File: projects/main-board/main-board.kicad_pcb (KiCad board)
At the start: 2 copper layers, 1 part, among them J4 TC2030

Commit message: Add footprints and 3D models
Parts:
- added J5: NHD-4.3-480272EF-ASXP (Molex 54104-4031), footprint-library:Molex 54104-4031, F.Cu at (134.6, 64.8)

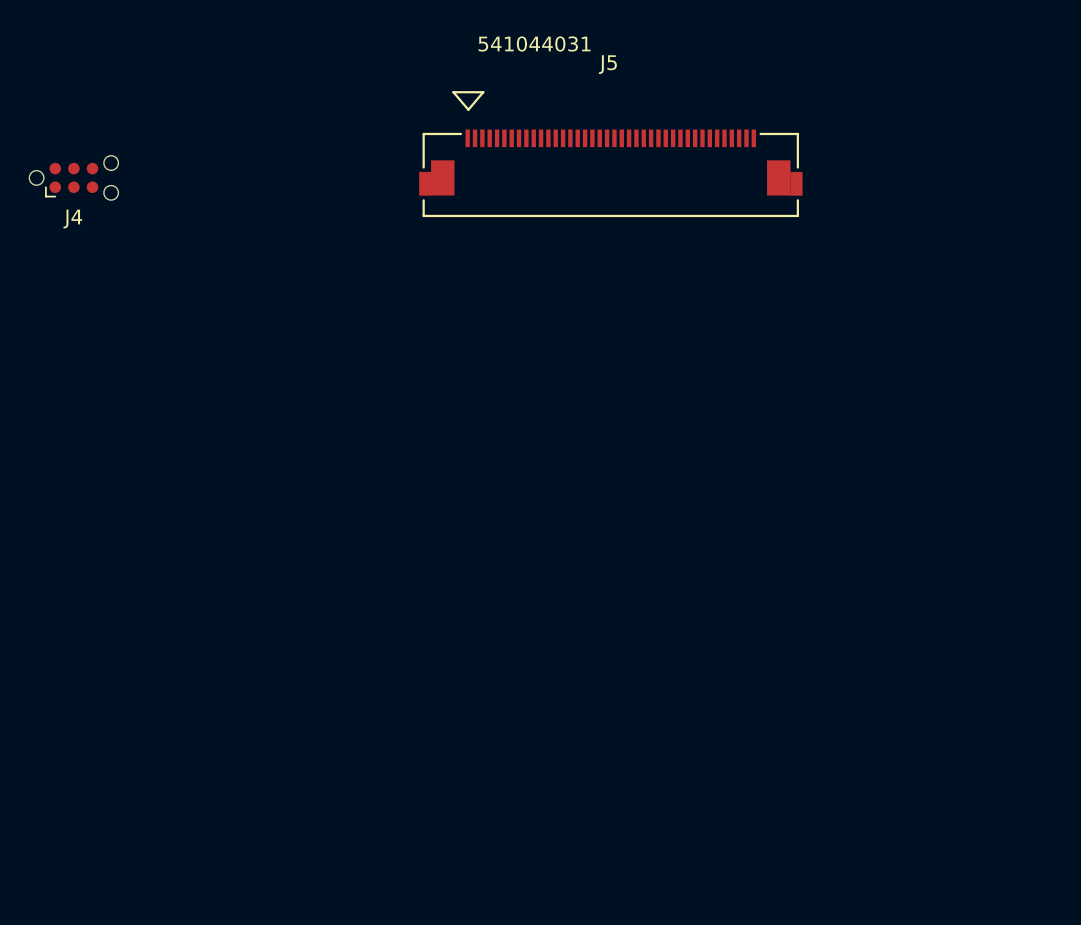
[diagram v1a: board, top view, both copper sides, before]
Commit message: Re-annotate schematics.
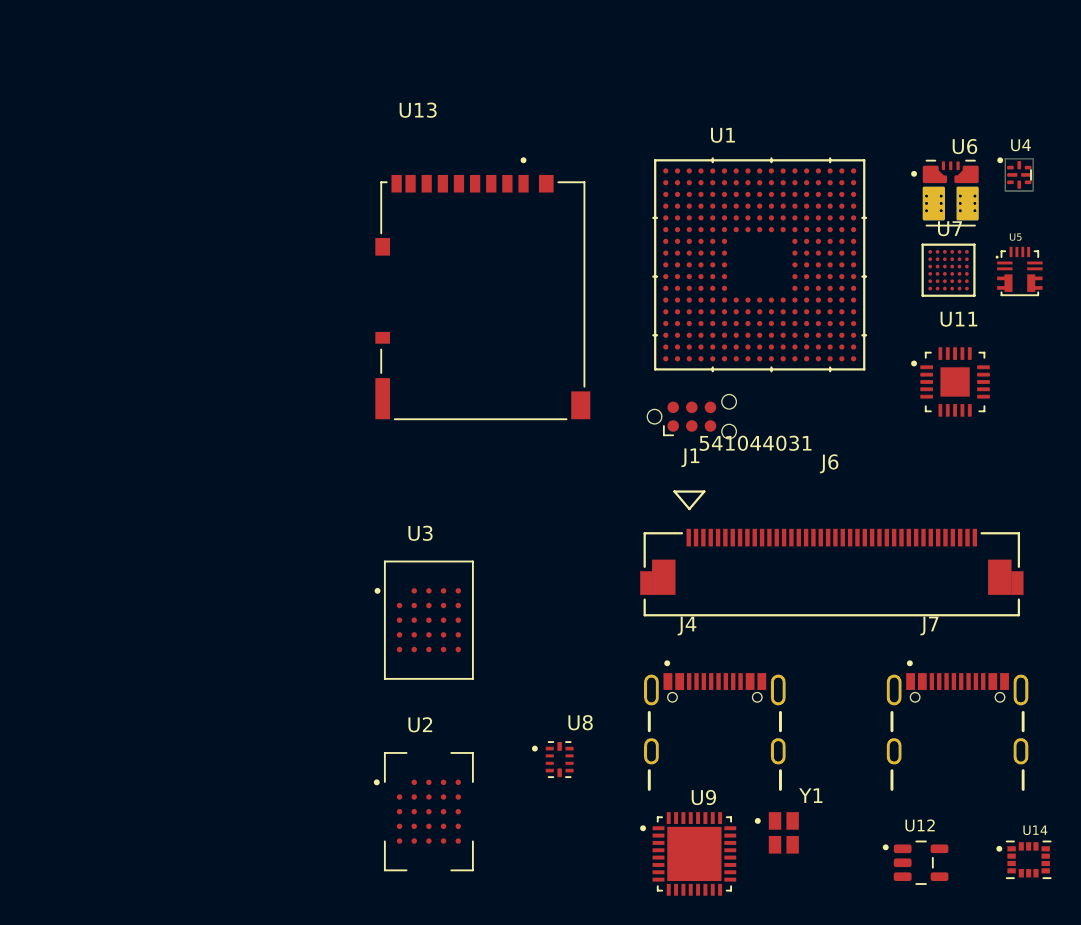
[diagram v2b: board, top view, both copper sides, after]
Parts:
- removed J5: NHD-4.3-480272EF-ASXP (Molex 54104-4031), footprint-library:Molex 54104-4031
- added J1: TC2030, Connector:Tag-Connect_TC2030-IDC-NL_2x03_P1.27mm_Vertical, F.Cu at (140.1, 81.3)
- added J6: NHD-4.3-480272EF-ASXP (Molex 54104-4031), footprint-library:Molex 54104-4031, F.Cu at (149.6, 92.0)
- added J7: USB4105-GF-A, footprint-library:USB4105-GF-A, F.Cu at (158.2, 104.1)
- added U1: STM32N657X0HxQ, footprint-library:STM32N645A0HxQ, F.Cu at (144.7, 70.9)
- added U11: NAU8325YG, footprint-library:NAU8325YG, F.Cu at (158.0, 78.9)
- added U12: TLV74330PDBVR, footprint-library:TLV74330PDBVR, F.Cu at (155.7, 111.7)
- added U13: DM3AT-SF-PEJM5, footprint-library:DM3AT-SF-PEJM5, F.Cu at (125.8, 73.4)
- added U14: LSM6DSO32TR, footprint-library:LSM6DSO32TR, F.Cu at (163.0, 111.5)
- added U2: APS256XXN-OBR-BG, footprint-library:APS256XXN-OBR-BG, F.Cu at (122.2, 108.2)
- added U3: MX25UM25645GXDI00, footprint-library:MX25UM25645GXDI00, F.Cu at (122.2, 95.1)
- added U4: TPS22992RXPR, footprint-library:TPS22992RXPR, F.Cu at (162.4, 64.8)
- added U5: MPM3805GQB-18-Z, footprint-library:MPM3805GQB-18-Z, F.Cu at (162.4, 71.5)
- added U6: TPSM863253RDXR, footprint-library:TPSM863253RDXR, F.Cu at (157.7, 66.1)
- added U7: MAX77972EWX+T, footprint-library:MAX77972EWX+T, F.Cu at (157.6, 71.3)
- added U8: TS3USB221ARSER, footprint-library:TS3USB221ARSER, F.Cu at (131.1, 104.6)
- added U9: ESP32-C6FH4, footprint-library:ESP32-C6FH4, F.Cu at (140.2, 111.1)
- added Y1: ABM10W-40.0000MHZ-8-B1U-T3, footprint-library:XTAL_ABM10W-40.0000MHZ-8-B1U-T3, F.Cu at (146.3, 109.6)
- J4: value TC2030 -> USB4105-GF-A; footprint Connector:Tag-Connect_TC2030-IDC-NL_2x03_P1.27mm_Vertical -> footprint-library:USB4105-GF-A
- moved J4 58.6 mm to (141.6, 104.1)

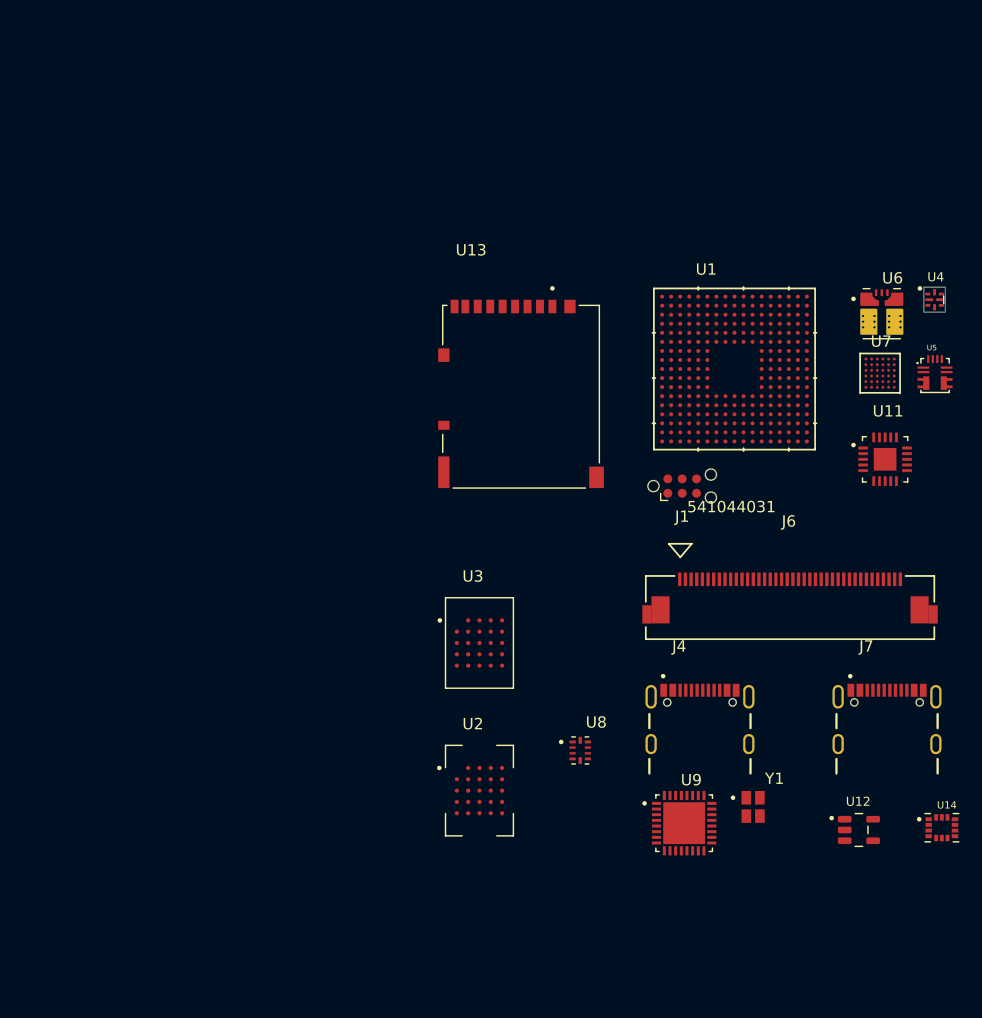
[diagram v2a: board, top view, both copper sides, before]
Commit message: Add footprints
- Inductors
- Switches
- Buttons
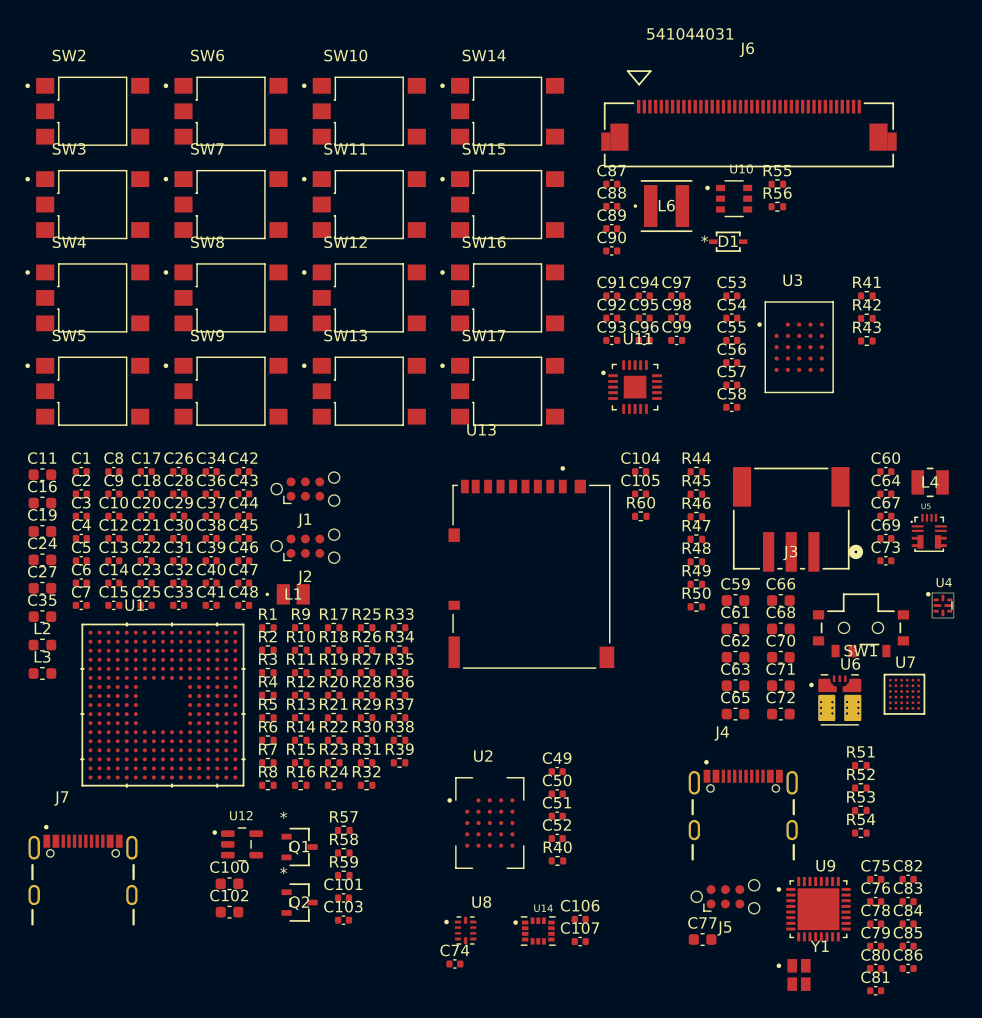
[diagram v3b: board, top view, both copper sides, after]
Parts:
- added C1: 100nF 10V, Capacitor_SMD:C_0402_1005Metric, F.Cu at (87.0, 80.0)
- added C10: 100nF 10V, Capacitor_SMD:C_0402_1005Metric, F.Cu at (89.8, 83.9)
- added C100: 10uF 10V, Capacitor_SMD:C_0603_1608Metric, F.Cu at (100.1, 116.4)
- added C101: 100nF 10V, Capacitor_SMD:C_0402_1005Metric, F.Cu at (110.1, 117.7)
- added C102: 10uF 10V, Capacitor_SMD:C_0603_1608Metric, F.Cu at (100.1, 118.9)
- added C103: 100nF 10V, Capacitor_SMD:C_0402_1005Metric, F.Cu at (110.1, 119.6)
- added C104: 100nF 10V, Capacitor_SMD:C_0402_1005Metric, F.Cu at (136.4, 80.0)
- added C105: 100nF 10V, Capacitor_SMD:C_0402_1005Metric, F.Cu at (136.4, 82.0)
- added C106: 100nF 10V, Capacitor_SMD:C_0402_1005Metric, F.Cu at (131.1, 119.5)
- added C107: 100nF 10V, Capacitor_SMD:C_0402_1005Metric, F.Cu at (131.1, 121.5)
- added C11: 22uF 10V, Capacitor_SMD:C_0603_1608Metric, F.Cu at (83.5, 80.2)
- added C12: 100nF 10V, Capacitor_SMD:C_0402_1005Metric, F.Cu at (89.8, 85.9)
- added C13: 100nF 10V, Capacitor_SMD:C_0402_1005Metric, F.Cu at (89.8, 87.9)
- added C14: 100nF 10V, Capacitor_SMD:C_0402_1005Metric, F.Cu at (89.8, 89.8)
- added C15: 100nF 10V, Capacitor_SMD:C_0402_1005Metric, F.Cu at (89.8, 91.8)
- added C16: 10uF 10V, Capacitor_SMD:C_0603_1608Metric, F.Cu at (83.5, 82.8)
- added C17: 1uF 10V, Capacitor_SMD:C_0402_1005Metric, F.Cu at (92.7, 80.0)
- added C18: 100nF 10V, Capacitor_SMD:C_0402_1005Metric, F.Cu at (92.7, 82.0)
- added C19: 22uF 10V, Capacitor_SMD:C_0603_1608Metric, F.Cu at (83.5, 85.3)
- added C2: 1uF 10V, Capacitor_SMD:C_0402_1005Metric, F.Cu at (87.0, 82.0)
- added C20: 1uF 10V, Capacitor_SMD:C_0402_1005Metric, F.Cu at (92.7, 83.9)
- added C21: 100nF 10V, Capacitor_SMD:C_0402_1005Metric, F.Cu at (92.7, 85.9)
- added C22: 1uF 10V, Capacitor_SMD:C_0402_1005Metric, F.Cu at (92.7, 87.9)
- added C23: 100nF 10V, Capacitor_SMD:C_0402_1005Metric, F.Cu at (92.7, 89.8)
- added C24: 10uF 10V, Capacitor_SMD:C_0603_1608Metric, F.Cu at (83.5, 87.8)
- added C25: 100nF 10V, Capacitor_SMD:C_0402_1005Metric, F.Cu at (92.7, 91.8)
- added C26: 100nF 10V, Capacitor_SMD:C_0402_1005Metric, F.Cu at (95.6, 80.0)
- added C27: 22uF 10V, Capacitor_SMD:C_0603_1608Metric, F.Cu at (83.5, 90.3)
- added C28: 100nF 10V, Capacitor_SMD:C_0402_1005Metric, F.Cu at (95.6, 82.0)
- added C29: 100nF 10V, Capacitor_SMD:C_0402_1005Metric, F.Cu at (95.6, 83.9)
- added C3: 2.2nF 10V, Capacitor_SMD:C_0402_1005Metric, F.Cu at (87.0, 83.9)
- added C30: 1uF 10V, Capacitor_SMD:C_0402_1005Metric, F.Cu at (95.6, 85.9)
- added C31: 100nF 10V, Capacitor_SMD:C_0402_1005Metric, F.Cu at (95.6, 87.9)
- added C32: 1uF 10V, Capacitor_SMD:C_0402_1005Metric, F.Cu at (95.6, 89.8)
- added C33: 100nF 10V, Capacitor_SMD:C_0402_1005Metric, F.Cu at (95.6, 91.8)
- added C34: 100nF 10V, Capacitor_SMD:C_0402_1005Metric, F.Cu at (98.4, 80.0)
- added C35: 22uF 10V, Capacitor_SMD:C_0603_1608Metric, F.Cu at (83.5, 92.8)
- added C36: 1uF 10V, Capacitor_SMD:C_0402_1005Metric, F.Cu at (98.4, 82.0)
- added C37: 1uF 10V, Capacitor_SMD:C_0402_1005Metric, F.Cu at (98.4, 83.9)
- added C38: 1uF 10V, Capacitor_SMD:C_0402_1005Metric, F.Cu at (98.4, 85.9)
- added C39: 1uF 10V, Capacitor_SMD:C_0402_1005Metric, F.Cu at (98.4, 87.9)
- added C4: 4.7uF 10V, Capacitor_SMD:C_0402_1005Metric, F.Cu at (87.0, 85.9)
- added C40: 100nF 10V, Capacitor_SMD:C_0402_1005Metric, F.Cu at (98.4, 89.8)
- added C41: 100nF 10V, Capacitor_SMD:C_0402_1005Metric, F.Cu at (98.4, 91.8)
- added C42: 100nF 10V, Capacitor_SMD:C_0402_1005Metric, F.Cu at (101.3, 80.0)
- added C43: 1uF 10V, Capacitor_SMD:C_0402_1005Metric, F.Cu at (101.3, 82.0)
- added C44: 100nF 10V, Capacitor_SMD:C_0402_1005Metric, F.Cu at (101.3, 83.9)
- added C45: 100nF 10V, Capacitor_SMD:C_0402_1005Metric, F.Cu at (101.3, 85.9)
- added C46: 1uF 10V, Capacitor_SMD:C_0402_1005Metric, F.Cu at (101.3, 87.9)
- added C47: 100nF 10V, Capacitor_SMD:C_0402_1005Metric, F.Cu at (101.3, 89.8)
- added C48: 1uF 10V, Capacitor_SMD:C_0402_1005Metric, F.Cu at (101.3, 91.8)
- added C49: 100nF 10V, Capacitor_SMD:C_0402_1005Metric, F.Cu at (129.0, 106.5)
- added C5: 100nF 10V, Capacitor_SMD:C_0402_1005Metric, F.Cu at (87.0, 87.9)
- added C50: 100nF 10V, Capacitor_SMD:C_0402_1005Metric, F.Cu at (129.0, 108.5)
- added C51: 4.7uF 10V, Capacitor_SMD:C_0402_1005Metric, F.Cu at (129.0, 110.4)
- added C52: 4.7uF 10V, Capacitor_SMD:C_0402_1005Metric, F.Cu at (129.0, 112.4)
- added C53: 4.7uF 10V, Capacitor_SMD:C_0402_1005Metric, F.Cu at (144.5, 64.4)
- added C54: 4.7uF 10V, Capacitor_SMD:C_0402_1005Metric, F.Cu at (144.5, 66.4)
- added C55: 4.7uF 10V, Capacitor_SMD:C_0402_1005Metric, F.Cu at (144.5, 68.4)
- added C56: 100nF 10V, Capacitor_SMD:C_0402_1005Metric, F.Cu at (144.5, 70.3)
- added C57: 100nF 10V, Capacitor_SMD:C_0402_1005Metric, F.Cu at (144.5, 72.3)
- added C58: 100nF 10V, Capacitor_SMD:C_0402_1005Metric, F.Cu at (144.5, 74.3)
- added C59: 10uF 10V, Capacitor_SMD:C_0603_1608Metric, F.Cu at (144.8, 91.4)
- added C6: 100nF 10V, Capacitor_SMD:C_0402_1005Metric, F.Cu at (87.0, 89.8)
- added C60: 100nF 10V, Capacitor_SMD:C_0402_1005Metric, F.Cu at (158.1, 80.0)
- added C61: 10uF 10V, Capacitor_SMD:C_0603_1608Metric, F.Cu at (144.8, 93.9)
- added C62: 10uF 10V, Capacitor_SMD:C_0603_1608Metric, F.Cu at (144.8, 96.4)
- added C63: 10uF 10V, Capacitor_SMD:C_0603_1608Metric, F.Cu at (144.8, 98.9)
- added C64: 2.2uF 10V, Capacitor_SMD:C_0402_1005Metric, F.Cu at (158.1, 82.0)
- added C65: 10uF 10V, Capacitor_SMD:C_0603_1608Metric, F.Cu at (144.8, 101.4)
- added C66: 10uF 10V, Capacitor_SMD:C_0603_1608Metric, F.Cu at (148.8, 91.4)
- added C67: 100nF 10V, Capacitor_SMD:C_0402_1005Metric, F.Cu at (158.1, 83.9)
- added C68: 10uF 10V, Capacitor_SMD:C_0603_1608Metric, F.Cu at (148.8, 93.9)
- added C69: 2.2uF 10V, Capacitor_SMD:C_0402_1005Metric, F.Cu at (158.1, 85.9)
- added C7: 100nF 10V, Capacitor_SMD:C_0402_1005Metric, F.Cu at (87.0, 91.8)
- added C70: 10uF 10V, Capacitor_SMD:C_0603_1608Metric, F.Cu at (148.8, 96.4)
- added C71: 10uF 10V, Capacitor_SMD:C_0603_1608Metric, F.Cu at (148.8, 98.9)
- added C72: 22uF 10V, Capacitor_SMD:C_0603_1608Metric, F.Cu at (148.8, 101.4)
- added C73: 2.2uF 10V, Capacitor_SMD:C_0402_1005Metric, F.Cu at (158.1, 87.9)
- added C74: 100nF 10V, Capacitor_SMD:C_0402_1005Metric, F.Cu at (120.0, 123.5)
- added C75: 1uF 10V, Capacitor_SMD:C_0402_1005Metric, F.Cu at (157.2, 116.0)
- added C76: 100nF 10V, Capacitor_SMD:C_0402_1005Metric, F.Cu at (157.2, 118.0)
- added C77: 10uF 10V, Capacitor_SMD:C_0603_1608Metric, F.Cu at (141.9, 121.3)
- added C78: 1uF 10V, Capacitor_SMD:C_0402_1005Metric, F.Cu at (157.2, 120.0)
- added C79: 100nF 10V, Capacitor_SMD:C_0402_1005Metric, F.Cu at (157.2, 121.9)
- added C8: 100nF 10V, Capacitor_SMD:C_0402_1005Metric, F.Cu at (89.8, 80.0)
- added C80: 100nF 10V, Capacitor_SMD:C_0402_1005Metric, F.Cu at (157.2, 123.9)
- added C81: 100nF 10V, Capacitor_SMD:C_0402_1005Metric, F.Cu at (157.2, 125.9)
- added C82: 100nF 10V, Capacitor_SMD:C_0402_1005Metric, F.Cu at (160.1, 116.0)
- added C83: 8pF 50V, Capacitor_SMD:C_0402_1005Metric, F.Cu at (160.1, 118.0)
- added C84: 100nF 10V, Capacitor_SMD:C_0402_1005Metric, F.Cu at (160.1, 120.0)
- added C85: 100nF 10V, Capacitor_SMD:C_0402_1005Metric, F.Cu at (160.1, 121.9)
- added C86: 8pF 50V, Capacitor_SMD:C_0402_1005Metric, F.Cu at (160.1, 123.9)
- added C87: 1uF 10V, Capacitor_SMD:C_0402_1005Metric, F.Cu at (133.8, 54.6)
- added C88: 1uF 10V, Capacitor_SMD:C_0402_1005Metric, F.Cu at (133.8, 56.5)
- added C89: 1uF 10V, Capacitor_SMD:C_0402_1005Metric, F.Cu at (133.8, 58.5)
- added C9: 1uF 10V, Capacitor_SMD:C_0402_1005Metric, F.Cu at (89.8, 82.0)
- added C90: 100nF 10V, Capacitor_SMD:C_0402_1005Metric, F.Cu at (133.8, 60.5)
- added C91: 4.7uF 10V, Capacitor_SMD:C_0402_1005Metric, F.Cu at (133.8, 64.4)
- added C92: 4.7uF 10V, Capacitor_SMD:C_0402_1005Metric, F.Cu at (133.8, 66.4)
- added C93: 100nF 10V, Capacitor_SMD:C_0402_1005Metric, F.Cu at (133.8, 68.4)
- added C94: 4.7uF 10V, Capacitor_SMD:C_0402_1005Metric, F.Cu at (136.7, 64.4)
- added C95: 100nF 10V, Capacitor_SMD:C_0402_1005Metric, F.Cu at (136.7, 66.4)
- added C96: 100nF 10V, Capacitor_SMD:C_0402_1005Metric, F.Cu at (136.7, 68.4)
- added C97: 100nF 10V, Capacitor_SMD:C_0402_1005Metric, F.Cu at (139.6, 64.4)
- added C98: 100nF 10V, Capacitor_SMD:C_0402_1005Metric, F.Cu at (139.6, 66.4)
- added C99: 4.7uF 10V, Capacitor_SMD:C_0402_1005Metric, F.Cu at (139.6, 68.4)
- added D1: B0540WS-7, footprint-library:SOD323_DIO, F.Cu at (144.1, 59.7)
- added J2: TC2030, Connector:Tag-Connect_TC2030-IDC-NL_2x03_P1.27mm_Vertical, F.Cu at (106.8, 86.6)
- added J3: S3B-PH-SM4-TB, footprint-library:S3B-PH-SM4-TB, F.Cu at (149.7, 84.1)
- added J5: TC2030, Connector:Tag-Connect_TC2030-IDC-NL_2x03_P1.27mm_Vertical, F.Cu at (143.9, 117.6)
- added L1: 1uH 2.7A 0.054R, footprint-library:IND_0806, F.Cu at (105.7, 90.8)
- added L2: 18R, Inductor_SMD:L_0603_1608Metric, F.Cu at (83.5, 95.3)
- added L3: 2.2nH 1.4A 0.018R, Inductor_SMD:L_0603_1608Metric, F.Cu at (83.5, 97.8)
- added L4: 470nH 4.3A 0.025R, footprint-library:HMLQ25201T-R47MSR, F.Cu at (162.0, 80.9)
- added L6: 22uH 540mA 0.576R, footprint-library:NR4012T220M, F.Cu at (138.7, 56.5)
- added Q1: ZXTN4240F-7, footprint-library:SOT23_ZXTN_DIO, F.Cu at (106.3, 113.2)
- added Q2: ZXTN4240F-7, footprint-library:SOT23_ZXTN_DIO, F.Cu at (106.3, 118.1)
- added R1: 2R, Resistor_SMD:R_0402_1005Metric, F.Cu at (103.5, 93.8)
- added R10: 0R, Resistor_SMD:R_0402_1005Metric, F.Cu at (106.4, 95.8)
- added R11: 0R, Resistor_SMD:R_0402_1005Metric, F.Cu at (106.4, 97.8)
- added R12: 0R, Resistor_SMD:R_0402_1005Metric, F.Cu at (106.4, 99.8)
- added R13: 0R, Resistor_SMD:R_0402_1005Metric, F.Cu at (106.4, 101.7)
- added R14: 0R, Resistor_SMD:R_0402_1005Metric, F.Cu at (106.4, 103.7)
- added R15: 0R, Resistor_SMD:R_0402_1005Metric, F.Cu at (106.4, 105.7)
- added R16: 0R, Resistor_SMD:R_0402_1005Metric, F.Cu at (106.4, 107.7)
- added R17: 0R, Resistor_SMD:R_0402_1005Metric, F.Cu at (109.3, 93.8)
- added R18: 0R, Resistor_SMD:R_0402_1005Metric, F.Cu at (109.3, 95.8)
- added R19: 0R, Resistor_SMD:R_0402_1005Metric, F.Cu at (109.3, 97.8)
- added R2: 200R, Resistor_SMD:R_0402_1005Metric, F.Cu at (103.5, 95.8)
- added R20: 0R, Resistor_SMD:R_0402_1005Metric, F.Cu at (109.3, 99.8)
- added R21: 0R, Resistor_SMD:R_0402_1005Metric, F.Cu at (109.3, 101.7)
- added R22: 0R, Resistor_SMD:R_0402_1005Metric, F.Cu at (109.3, 103.7)
- added R23: 0R, Resistor_SMD:R_0402_1005Metric, F.Cu at (109.3, 105.7)
- added R24: 0R, Resistor_SMD:R_0402_1005Metric, F.Cu at (109.3, 107.7)
- added R25: 0R, Resistor_SMD:R_0402_1005Metric, F.Cu at (112.2, 93.8)
- added R26: 0R, Resistor_SMD:R_0402_1005Metric, F.Cu at (112.2, 95.8)
- added R27: 0R, Resistor_SMD:R_0402_1005Metric, F.Cu at (112.2, 97.8)
- added R28: 0R, Resistor_SMD:R_0402_1005Metric, F.Cu at (112.2, 99.8)
- added R29: 0R, Resistor_SMD:R_0402_1005Metric, F.Cu at (112.2, 101.7)
- added R3: 10K, Resistor_SMD:R_0402_1005Metric, F.Cu at (103.5, 97.8)
- added R30: 0R, Resistor_SMD:R_0402_1005Metric, F.Cu at (112.2, 103.7)
- added R31: 0R, Resistor_SMD:R_0402_1005Metric, F.Cu at (112.2, 105.7)
- added R32: 0R, Resistor_SMD:R_0402_1005Metric, F.Cu at (112.2, 107.7)
- added R33: 0R, Resistor_SMD:R_0402_1005Metric, F.Cu at (115.1, 93.8)
- added R34: 0R, Resistor_SMD:R_0402_1005Metric, F.Cu at (115.1, 95.8)
- added R35: 0R, Resistor_SMD:R_0402_1005Metric, F.Cu at (115.1, 97.8)
- added R36: 0R, Resistor_SMD:R_0402_1005Metric, F.Cu at (115.1, 99.8)
- added R37: 0R, Resistor_SMD:R_0402_1005Metric, F.Cu at (115.1, 101.7)
- added R38: 0R, Resistor_SMD:R_0402_1005Metric, F.Cu at (115.1, 103.7)
- added R39: 0R, Resistor_SMD:R_0402_1005Metric, F.Cu at (115.1, 105.7)
- added R4: 50.1K, Resistor_SMD:R_0402_1005Metric, F.Cu at (103.5, 99.8)
- added R40: 10K, Resistor_SMD:R_0402_1005Metric, F.Cu at (129.1, 114.4)
- added R41: 10K, Resistor_SMD:R_0402_1005Metric, F.Cu at (156.4, 64.5)
- added R42: 10K, Resistor_SMD:R_0402_1005Metric, F.Cu at (156.4, 66.4)
- added R43: 10K, Resistor_SMD:R_0402_1005Metric, F.Cu at (156.4, 68.4)
- added R44: 100R, Resistor_SMD:R_0402_1005Metric, F.Cu at (141.3, 80.0)
- added R45: 10K, Resistor_SMD:R_0402_1005Metric, F.Cu at (141.3, 82.0)
- added R46: 10K, Resistor_SMD:R_0402_1005Metric, F.Cu at (141.3, 84.0)
- added R47: 10K, Resistor_SMD:R_0402_1005Metric, F.Cu at (141.3, 86.0)
- added R48: 6.34K, Resistor_SMD:R_0402_1005Metric, F.Cu at (141.3, 88.0)
- added R49: 4.42K, Resistor_SMD:R_0402_1005Metric, F.Cu at (141.3, 89.9)
- added R5: 2.2K, Resistor_SMD:R_0402_1005Metric, F.Cu at (103.5, 101.7)
- added R50: 0.01R, Resistor_SMD:R_0402_1005Metric, F.Cu at (141.3, 91.9)
- added R51: 5.1K, Resistor_SMD:R_0402_1005Metric, F.Cu at (155.9, 106.0)
- added R52: 10K, Resistor_SMD:R_0402_1005Metric, F.Cu at (155.9, 108.0)
- added R53: 5.1K, Resistor_SMD:R_0402_1005Metric, F.Cu at (155.9, 109.9)
- added R54: 0R, Resistor_SMD:R_0402_1005Metric, F.Cu at (155.9, 111.9)
- added R55: 10K, Resistor_SMD:R_0402_1005Metric, F.Cu at (148.5, 54.6)
- added R56: 6.81R, Resistor_SMD:R_0402_1005Metric, F.Cu at (148.5, 56.6)
- added R57: 10K, Resistor_SMD:R_0402_1005Metric, F.Cu at (110.2, 111.7)
- added R58: 1K, Resistor_SMD:R_0402_1005Metric, F.Cu at (110.2, 113.7)
- added R59: 1K, Resistor_SMD:R_0402_1005Metric, F.Cu at (110.2, 115.7)
- added R6: 2.2K, Resistor_SMD:R_0402_1005Metric, F.Cu at (103.5, 103.7)
- added R60: 10K, Resistor_SMD:R_0402_1005Metric, F.Cu at (136.4, 83.9)
- added R7: 2.2K, Resistor_SMD:R_0402_1005Metric, F.Cu at (103.5, 105.7)
- added R8: 2.2K, Resistor_SMD:R_0402_1005Metric, F.Cu at (103.5, 107.7)
- added R9: 0R, Resistor_SMD:R_0402_1005Metric, F.Cu at (106.4, 93.8)
- added SW1: 450404015514, footprint-library:450404015514, F.Cu at (155.9, 93.8)
- added SW10: TS06-667-25-BK-160-G-SMT-TR, footprint-library:TS06-667-25-BK-160-G-SMT-TR, F.Cu at (112.4, 48.1)
- added SW11: TS06-667-25-BK-160-G-SMT-TR, footprint-library:TS06-667-25-BK-160-G-SMT-TR, F.Cu at (112.4, 56.4)
- added SW12: TS06-667-25-BK-160-G-SMT-TR, footprint-library:TS06-667-25-BK-160-G-SMT-TR, F.Cu at (112.4, 64.6)
- added SW13: TS06-667-25-BK-160-G-SMT-TR, footprint-library:TS06-667-25-BK-160-G-SMT-TR, F.Cu at (112.4, 72.9)
- added SW14: TS06-667-25-BK-160-G-SMT-TR, footprint-library:TS06-667-25-BK-160-G-SMT-TR, F.Cu at (124.6, 48.1)
- added SW15: TS06-667-25-BK-160-G-SMT-TR, footprint-library:TS06-667-25-BK-160-G-SMT-TR, F.Cu at (124.6, 56.4)
- added SW16: TS06-667-25-BK-160-G-SMT-TR, footprint-library:TS06-667-25-BK-160-G-SMT-TR, F.Cu at (124.6, 64.6)
- added SW17: TS06-667-25-BK-160-G-SMT-TR, footprint-library:TS06-667-25-BK-160-G-SMT-TR, F.Cu at (124.6, 72.9)
- added SW2: TS06-667-25-BK-160-G-SMT-TR, footprint-library:TS06-667-25-BK-160-G-SMT-TR, F.Cu at (88.0, 48.1)
- added SW3: TS06-667-25-BK-160-G-SMT-TR, footprint-library:TS06-667-25-BK-160-G-SMT-TR, F.Cu at (88.0, 56.4)
- added SW4: TS06-667-25-BK-160-G-SMT-TR, footprint-library:TS06-667-25-BK-160-G-SMT-TR, F.Cu at (88.0, 64.6)
- added SW5: TS06-667-25-BK-160-G-SMT-TR, footprint-library:TS06-667-25-BK-160-G-SMT-TR, F.Cu at (88.0, 72.9)
- added SW6: TS06-667-25-BK-160-G-SMT-TR, footprint-library:TS06-667-25-BK-160-G-SMT-TR, F.Cu at (100.2, 48.1)
- added SW7: TS06-667-25-BK-160-G-SMT-TR, footprint-library:TS06-667-25-BK-160-G-SMT-TR, F.Cu at (100.2, 56.4)
- added SW8: TS06-667-25-BK-160-G-SMT-TR, footprint-library:TS06-667-25-BK-160-G-SMT-TR, F.Cu at (100.2, 64.6)
- added SW9: TS06-667-25-BK-160-G-SMT-TR, footprint-library:TS06-667-25-BK-160-G-SMT-TR, F.Cu at (100.2, 72.9)
- added U10: AP5725WG-7, footprint-library:AP5725WG-7, F.Cu at (144.7, 55.9)
- moved J7 72.3 mm to (87.1, 117.4)
- moved U1 58.6 mm to (94.2, 100.6)
- moved U12 54.5 mm to (101.2, 112.9)
- moved J6 41.9 mm to (146.0, 50.2)
- moved U3 38.5 mm to (150.4, 69.0)
- moved U14 36.8 mm to (127.4, 120.6)
- moved U6 34.3 mm to (154.0, 100.2)
- moved J1 33.3 mm to (106.8, 81.5)
- moved U7 28.5 mm to (159.7, 99.7)
- moved U4 27.0 mm to (163.1, 91.8)
- moved U11 23.0 mm to (135.9, 72.5)
- moved U8 18.9 mm to (120.9, 120.5)
- moved U13 15.9 mm to (126.7, 89.3)
- moved Y1 15.4 mm to (150.4, 124.5)
- moved U9 14.1 mm to (152.1, 118.7)
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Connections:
- net Net-(U11-SPK_LN) renamed /Audio/LEFT_SPEAKER_N
- net Net-(U11-SPK_LP) renamed /Audio/LEFT_SPEAKER_P
- net Net-(U11-SPK_RN) renamed /Audio/RIGHT_SPEAKER_P
- net Net-(U11-SPK_RP) renamed /Audio/RIGHT_SPEAKER_N
- U12 pad 5: Net-(M1-+) -> /Haptics/LEFT_MOTOR_P
- U13 pad 6: unconnected-(U13-VSS-Pad6) -> GND
- U7 pad A4: Net-(J3-Pin_2) -> /Power/BAT_NTC

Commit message: Add board design rules
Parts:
- moved J6 194.5 mm to (-39.0, 110.2), turned to -90 degrees
- moved R55 173.1 mm to (-24.6, 57.6)
- moved R56 173.1 mm to (-24.6, 59.6)
- moved C87 173.1 mm to (-39.2, 57.6)
- moved C88 173.1 mm to (-39.2, 59.5)
- moved D1 173.1 mm to (-28.9, 62.7)
- moved L6 173.1 mm to (-34.4, 59.5)
- moved U10 173.1 mm to (-28.4, 58.8)
- moved C89 165.8 mm to (-26.0, 102.5)
- moved C90 165.8 mm to (-26.0, 104.5)
- moved J4 154.3 mm to (154.7, 265.7)
- moved R51 152.6 mm to (153.4, 258.5), turned to 90 degrees
- moved R53 148.6 mm to (156.4, 258.5), turned to 90 degrees
- moved J7 127.9 mm to (59.1, 242.2)
- moved C75 122.9 mm to (201.1, 230.9)
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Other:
- copper layers 2 -> 4
- rule pad_to_mask_clearance: 0 -> 0.025

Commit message: Fix footprint DRC errors.
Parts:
- removed SW17: TS06-667-25-BK-160-G-SMT-TR, footprint-library:TS06-667-25-BK-160-G-SMT-TR
- added SW18: TS06-667-25-BK-160-G-SMT-TR, footprint-library:TS06-667-25-BK-160-G-SMT-TR, F.Cu at (110.8, -27.4)
- moved J7 32.3 mm to (52.5, 210.6)
- moved R57 22.5 mm to (31.7, 41.1), turned to 180 degrees
- moved C101 18.8 mm to (32.0, 38.6), turned to 180 degrees
- moved SW10 17.6 mm to (98.6, -52.2)
- moved SW11 17.6 mm to (98.6, -44.0)
- moved SW12 17.6 mm to (98.6, -35.7)
- moved SW14 17.6 mm to (110.8, -52.2)
- moved SW15 17.6 mm to (110.8, -44.0)
- moved SW16 17.6 mm to (110.8, -35.7)
- moved SW2 17.6 mm to (74.1, -52.2)
- moved SW3 17.6 mm to (74.1, -44.0)
- moved SW4 17.6 mm to (74.1, -35.7)
- moved SW6 17.6 mm to (86.3, -52.2)
- moved SW7 17.6 mm to (86.3, -44.0)
- moved SW8 17.6 mm to (86.3, -35.7)
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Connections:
- net /Haptics/LEFT_MOTOR_P renamed /Haptics/MOTOR_P
- J4 pad SH1: (no net) -> GND
- J4 pad SH2: (no net) -> GND
- J4 pad SH3: (no net) -> GND
- J4 pad SH4: (no net) -> GND
- J6 pad P1: (no net) -> GND
- J6 pad P2: (no net) -> GND
- J7 pad SH1: (no net) -> GND
- J7 pad SH2: (no net) -> GND
- J7 pad SH3: (no net) -> GND
- J7 pad SH4: (no net) -> GND
- R60 pad 2: /MCU/SD.DETECT -> Net-(U13-DETECT_B)
- SW1 pad 4: (no net) -> GND
- SW10 pad 1: /Buttons/BUTTONS.B8 -> /Buttons/BUTTONS.B9
- SW10 pad 3: /Buttons/BUTTONS.B8 -> /Buttons/BUTTONS.B9
- SW10 pad 5: (no net) -> GND
- SW11 pad 1: /Buttons/BUTTONS.B9 -> /Buttons/BUTTONS.B10
- SW11 pad 3: /Buttons/BUTTONS.B9 -> /Buttons/BUTTONS.B10
- SW11 pad 5: (no net) -> GND
- SW12 pad 1: /Buttons/BUTTONS.B10 -> /Buttons/BUTTONS.B11
- SW12 pad 3: /Buttons/BUTTONS.B10 -> /Buttons/BUTTONS.B11
- SW12 pad 5: (no net) -> GND
- SW13 pad 1: /Buttons/BUTTONS.B11 -> /Buttons/BUTTONS.B12
- SW13 pad 3: /Buttons/BUTTONS.B11 -> /Buttons/BUTTONS.B12
- SW13 pad 5: (no net) -> GND
- SW14 pad 1: /Buttons/BUTTONS.B12 -> /Buttons/BUTTONS.B13
- SW14 pad 3: /Buttons/BUTTONS.B12 -> /Buttons/BUTTONS.B13
- SW14 pad 5: (no net) -> GND
- SW15 pad 1: /Buttons/BUTTONS.B13 -> /Buttons/BUTTONS.B14
- SW15 pad 3: /Buttons/BUTTONS.B13 -> /Buttons/BUTTONS.B14
- SW15 pad 5: (no net) -> GND
- SW16 pad 1: /Buttons/BUTTONS.B14 -> /Buttons/BUTTONS.B15
- SW16 pad 3: /Buttons/BUTTONS.B14 -> /Buttons/BUTTONS.B15
- SW16 pad 5: (no net) -> GND
- SW2 pad 1: /Buttons/BUTTONS.B0 -> /Buttons/BUTTONS.B1
- SW2 pad 3: /Buttons/BUTTONS.B0 -> /Buttons/BUTTONS.B1
- SW2 pad 5: (no net) -> GND
- SW3 pad 1: /Buttons/BUTTONS.B1 -> /Buttons/BUTTONS.B2
- SW3 pad 3: /Buttons/BUTTONS.B1 -> /Buttons/BUTTONS.B2
- SW3 pad 5: (no net) -> GND
- SW4 pad 1: /Buttons/BUTTONS.B2 -> /Buttons/BUTTONS.B3
- SW4 pad 3: /Buttons/BUTTONS.B2 -> /Buttons/BUTTONS.B3
- SW4 pad 5: (no net) -> GND
- SW5 pad 1: /Buttons/BUTTONS.B3 -> /Buttons/BUTTONS.B4
- SW5 pad 3: /Buttons/BUTTONS.B3 -> /Buttons/BUTTONS.B4
- SW5 pad 5: (no net) -> GND
- SW6 pad 1: /Buttons/BUTTONS.B4 -> /Buttons/BUTTONS.B5
- SW6 pad 3: /Buttons/BUTTONS.B4 -> /Buttons/BUTTONS.B5
- SW6 pad 5: (no net) -> GND
- SW7 pad 1: /Buttons/BUTTONS.B5 -> /Buttons/BUTTONS.B6
- SW7 pad 3: /Buttons/BUTTONS.B5 -> /Buttons/BUTTONS.B6
- SW7 pad 5: (no net) -> GND
- SW8 pad 1: /Buttons/BUTTONS.B6 -> /Buttons/BUTTONS.B7
- SW8 pad 3: /Buttons/BUTTONS.B6 -> /Buttons/BUTTONS.B7
- SW8 pad 5: (no net) -> GND
- SW9 pad 1: /Buttons/BUTTONS.B7 -> /Buttons/BUTTONS.B8
- SW9 pad 3: /Buttons/BUTTONS.B7 -> /Buttons/BUTTONS.B8
- SW9 pad 5: (no net) -> GND
- U14 pad 9: (no net) -> unconnected-(U14-INT2-Pad9)

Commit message: Rough PCB component grouping and layout
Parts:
- added C108: 2.2uF 10V, Capacitor_SMD:C_0402_1005Metric, F.Cu at (66.5, 241.5)
- moved SW10 254.5 mm to (-29.1, 167.9)
- moved SW11 254.5 mm to (-29.1, 176.2)
- moved SW12 254.5 mm to (-29.1, 184.4)
- moved SW13 254.5 mm to (-29.1, 192.7)
- moved SW14 254.5 mm to (-16.9, 167.9)
- moved SW15 254.5 mm to (-16.9, 176.2)
- moved SW16 254.5 mm to (-16.9, 184.4)
- moved SW18 254.5 mm to (-16.9, 192.7)
- moved SW2 254.5 mm to (-53.6, 167.9)
- moved SW3 254.5 mm to (-53.6, 176.2)
- moved SW4 254.5 mm to (-53.6, 184.4)
- moved SW5 254.5 mm to (-53.6, 192.7)
- moved SW6 254.5 mm to (-41.4, 167.9)
- moved SW7 254.5 mm to (-41.4, 176.2)
- moved SW8 254.5 mm to (-41.4, 184.4)
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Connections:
- R41 pad 2: /Flash/CS_N -> /Flash/FLASH_OCTOSPI.CS_N
- R42 pad 2: /Flash/RESET_N -> /Flash/FLASH_OCTOSPI.RESET_N
- U3 pad A4: /Flash/RESET_N -> /Flash/FLASH_OCTOSPI.RESET_N
- U3 pad B2: /Flash/SCLK -> /Flash/FLASH_OCTOSPI.SCLK
- U3 pad C2: /Flash/CS_N -> /Flash/FLASH_OCTOSPI.CS_N
- U3 pad C3: /Flash/DQS -> /Flash/FLASH_OCTOSPI.DQS
- U3 pad C4: /Flash/SIO2 -> /Flash/FLASH_OCTOSPI.SIO2
- U3 pad D2: /Flash/SIO1 -> /Flash/FLASH_OCTOSPI.SIO1
- U3 pad D3: /Flash/SIO0 -> /Flash/FLASH_OCTOSPI.SIO0
- U3 pad D4: /Flash/SIO3 -> /Flash/FLASH_OCTOSPI.SIO3
- U3 pad D5: /Flash/SIO4 -> /Flash/FLASH_OCTOSPI.SIO4
- U3 pad E1: /Flash/SIO7 -> /Flash/FLASH_OCTOSPI.SIO7
- U3 pad E2: /Flash/SIO6 -> /Flash/FLASH_OCTOSPI.SIO6
- U3 pad E3: /Flash/SIO5 -> /Flash/FLASH_OCTOSPI.SIO5
